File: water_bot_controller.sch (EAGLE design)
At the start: 103 parts, among them IC1 ULN2803A, U2 LM3480IM3-5.0

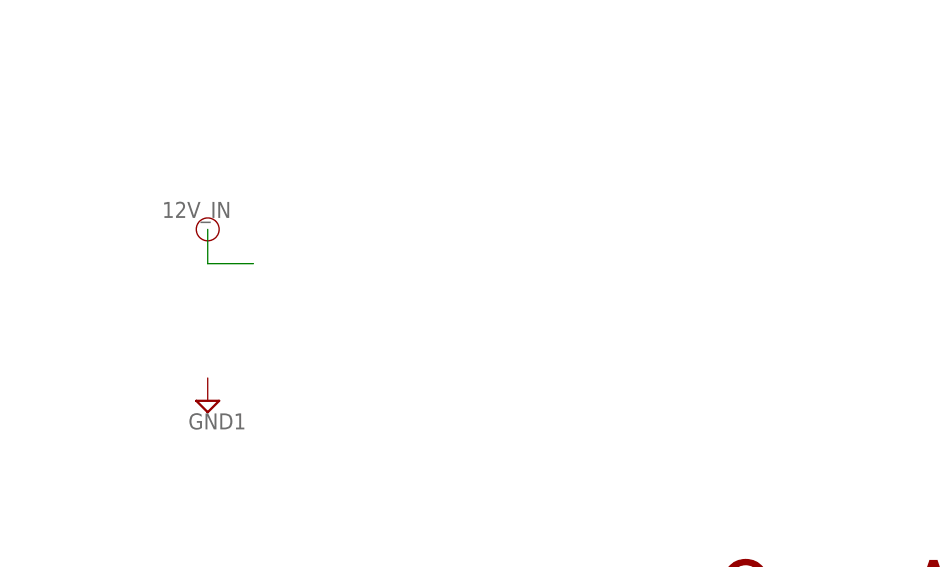
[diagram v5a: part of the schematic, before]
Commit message: added 12v power conditioning
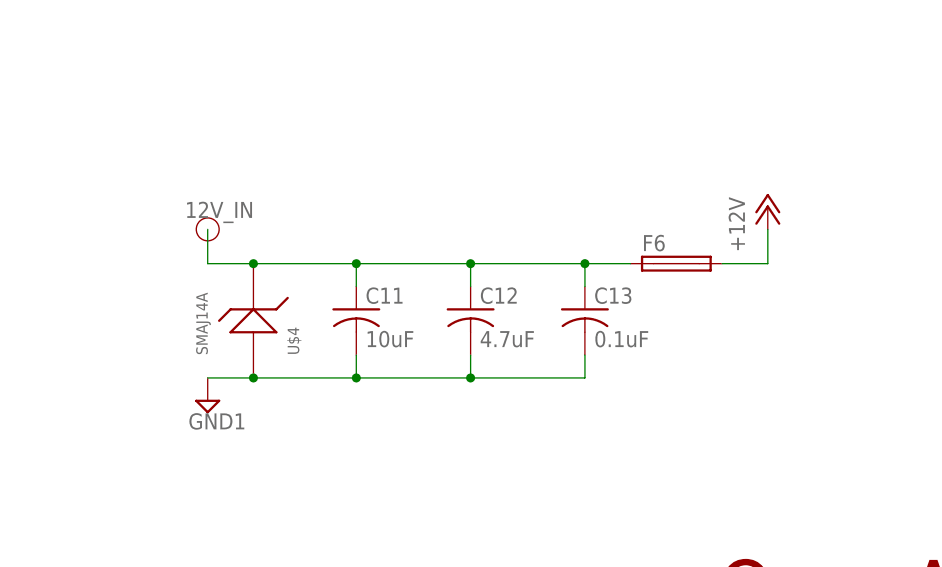
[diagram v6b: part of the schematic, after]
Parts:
- added C11: 10uF, rcl:C-USC1206
- added C12: 4.7uF, rcl:C-USC1206
- added C13: 0.1uF, rcl:C-USC0603
- added F6: (no value), fuse:GSH15
- added U$4: SMAJ14A, openag_diodes:SMAJ14A
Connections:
- net +12V: now also F6.2
- net 12V_IN: now also C11.1, C12.1, C13.1, F6.1, U$4.P$2
- net GND1: now also C11.2, C12.2, C13.2, U$4.P$1
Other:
- note added: "12V Input Power Conditioning"
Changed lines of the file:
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@@
 <part name="TP23" library="testpad" library_urn="urn:adsk.eagle:library:385" deviceset="PTR1" device="B2,54" package3d_urn="urn:adsk.eagle:package:27948/1"/>
 <part name="SUPPLY22" library="supply2" library_urn="urn:adsk.eagle:library:372" deviceset="GND1" device=""/>
+<part name="U$4" library="openag_diodes" deviceset="SMAJ14A" device=""/>
+<part name="C11" library="rcl" library_urn="urn:adsk.eagle:library:334" deviceset="C-US" device="C1206" package3d_urn="urn:adsk.eagle:package:23618/2" value="10uF"/>
+<part name="C12" library="rcl" library_urn="urn:adsk.eagle:library:334" deviceset="C-US" device="C1206" package3d_urn="urn:adsk.eagle:package:23618/2" value="4.7uF"/>
+<part name="C13" library="rcl" library_urn="urn:adsk.eagle:library:334" deviceset="C-US" device="C0603" package3d_urn="urn:adsk.eagle:package:23616/2" value="0.1uF"/>
+<part name="F6" library="fuse" library_urn="urn:adsk.eagle:library:233" deviceset="GSH15" device="" package3d_urn="urn:adsk.eagle:package:14065/1"/>
+<part name="P+8" library="supply1" library_urn="urn:adsk.eagle:library:371" deviceset="+12V" device=""/>
 </parts>
 <sheets>
@@
 <circle x="299.72" y="104.14" radius="1.27" width="0.1524" layer="94"/>
 <circle x="142.24" y="26.67" radius="1.27" width="0.1524" layer="94"/>
+<wire x1="137.16" y1="2.54" x2="208.28" y2="2.54" width="0.1524" layer="90" style="longdash"/>
+<wire x1="208.28" y1="2.54" x2="208.28" y2="35.56" width="0.1524" layer="90" style="longdash"/>
+<wire x1="208.28" y1="35.56" x2="137.16" y2="35.56" width="0.1524" layer="90" style="longdash"/>
+<wire x1="137.16" y1="35.56" x2="137.16" y2="2.54" width="0.1524" layer="90" style="longdash"/>
+<text x="151.13" y="30.48" size="2.54" layer="90">12V Input Power Conditioning</text>
 </plain>
 <instances>
@@
 <instance part="TP23" gate="G$1" x="361.95" y="102.87" rot="R180"/>
 <instance part="SUPPLY22" gate="G$1" x="142.24" y="7.62"/>
+<instance part="U$4" gate="G$1" x="147.32" y="17.78" rot="R90"/>
+<instance part="C11" gate="G$1" x="158.75" y="17.78"/>
+<instance part="C12" gate="G$1" x="171.45" y="17.78"/>
+<instance part="C13" gate="G$1" x="184.15" y="17.78"/>
+<instance part="F6" gate="1" x="194.31" y="22.86"/>
+<instance part="P+8" gate="1" x="204.47" y="29.21"/>
 </instances>
 <busses>
@@
 <wire x1="-44.45" y1="87.63" x2="-44.45" y2="100.33" width="0.1524" layer="91"/>
 <junction x="-44.45" y="100.33"/>
+</segment>
+<segment>
+<pinref part="F6" gate="1" pin="2"/>
+<wire x1="199.39" y1="22.86" x2="204.47" y2="22.86" width="0.1524" layer="91"/>
+<pinref part="P+8" gate="1" pin="+12V"/>
+<wire x1="204.47" y1="22.86" x2="204.47" y2="26.67" width="0.1524" layer="91"/>
 </segment>
 </net>
@@
 <wire x1="369.57" y1="52.07" x2="368.3" y2="52.07" width="0.1524" layer="91" style="longdash"/>
 </segment>
+<segment>
+<pinref part="SUPPLY22" gate="G$1" pin="GND1"/>
+<pinref part="U$4" gate="G$1" pin="P$1"/>
+<wire x1="142.24" y1="10.16" x2="147.32" y2="10.16" width="0.1524" layer="91"/>
+<pinref part="C11" gate="G$1" pin="2"/>
+<wire x1="158.75" y1="10.16" x2="158.75" y2="12.7" width="0.1524" layer="91"/>
+<pinref part="C12" gate="G$1" pin="2"/>
+<wire x1="158.75" y1="10.16" x2="171.45" y2="10.16" width="0.1524" layer="91"/>
+<wire x1="171.45" y1="10.16" x2="171.45" y2="12.7" width="0.1524" layer="91"/>
+<pinref part="C13" gate="G$1" pin="2"/>
+<wire x1="171.45" y1="10.16" x2="184.15" y2="10.16" width="0.1524" layer="91"/>
+<wire x1="184.15" y1="10.16" x2="184.15" y2="12.7" width="0.1524" layer="91"/>
+<junction x="171.45" y="10.16"/>
+<wire x1="147.32" y1="10.16" x2="158.75" y2="10.16" width="0.1524" layer="91"/>
+<junction x="147.32" y="10.16"/>
+<junction x="158.75" y="10.16"/>
+</segment>
 </net>
 <net name="GND2" class="0">
@@
 </segment>
 <segment>
-<wire x1="142.24" y1="26.67" x2="142.24" y2="22.86" width="0.1524" layer="91"/>
-<wire x1="142.24" y1="22.86" x2="147.32" y2="22.86" width="0.1524" layer="91"/>
-<label x="137.16" y="27.94" size="1.778" layer="95"/>
-</segment>
-</net>
+<pinref part="C11" gate="G$1" pin="1"/>
+<wire x1="158.75" y1="22.86" x2="158.75" y2="20.32" width="0.1524" layer="91"/>
+<pinref part="C12" gate="G$1" pin="1"/>
+<wire x1="158.75" y1="22.86" x2="171.45" y2="22.86" width="0.1524" layer="91"/>
+<wire x1="171.45" y1="22.86" x2="171.45" y2="20.32" width="0.1524" layer="91"/>
+<pinref part="C13" gate="G$1" pin="1"/>
+<wire x1="171.45" y1="22.86" x2="184.15" y2="22.86" width="0.1524" layer="91"/>
+<wire x1="184.15" y1="22.86" x2="184.15" y2="20.32" width="0.1524" layer="91"/>
+<junction x="171.45" y="22.86"/>
+<pinref part="F6" gate="1" pin="1"/>
+<wire x1="184.15" y1="22.86" x2="189.23" y2="22.86" width="0.1524" layer="91"/>
+<junction x="184.15" y="22.86"/>
+<pinref part="U$4" gate="G$1" pin="P$2"/>
+<wire x1="158.75" y1="22.86" x2="147.32" y2="22.86" width="0.1524" layer="91"/>
+<junction x="158.75" y="22.86"/>
+<wire x1="147.32" y1="22.86" x2="142.24" y2="22.86" width="0.1524" layer="91"/>
+<wire x1="142.24" y1="22.86" x2="142.24" y2="26.67" width="0.1524" layer="91"/>
+<junction x="147.32" y="22.86"/>
+<label x="139.7" y="27.94" size="1.778" layer="95"/>
+</segment>
+</net>
